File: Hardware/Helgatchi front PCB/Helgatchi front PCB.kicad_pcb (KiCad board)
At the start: 2 copper layers, 50 x 80 mm, 34 parts, among them J1 BATTERY, J2 SCREEN, M1 MOTOR, Q1 NMOS, SW1 LEFT BUTTON, SW2 CENTER BUTTON, SW3 RIGHT BUTTON, U1 XIAO ESP32-S3

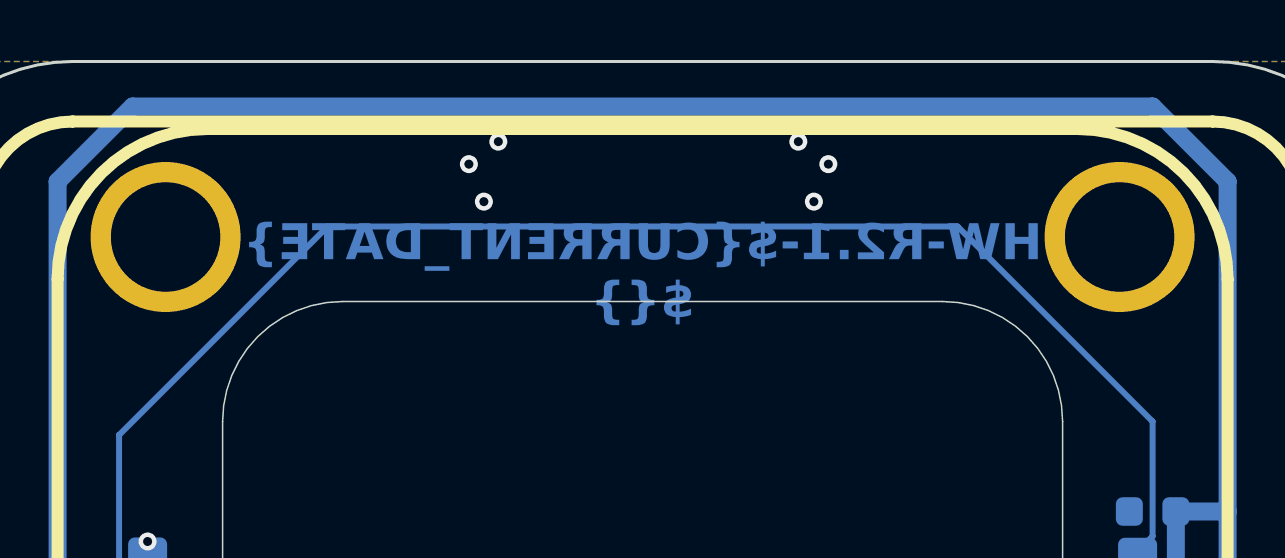
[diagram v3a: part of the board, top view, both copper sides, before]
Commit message: LCSC part # changes
- Changed MOLEX Picoblate part number out for generic picoblade
- Added part number and adjusted DNP for ESP32-S3
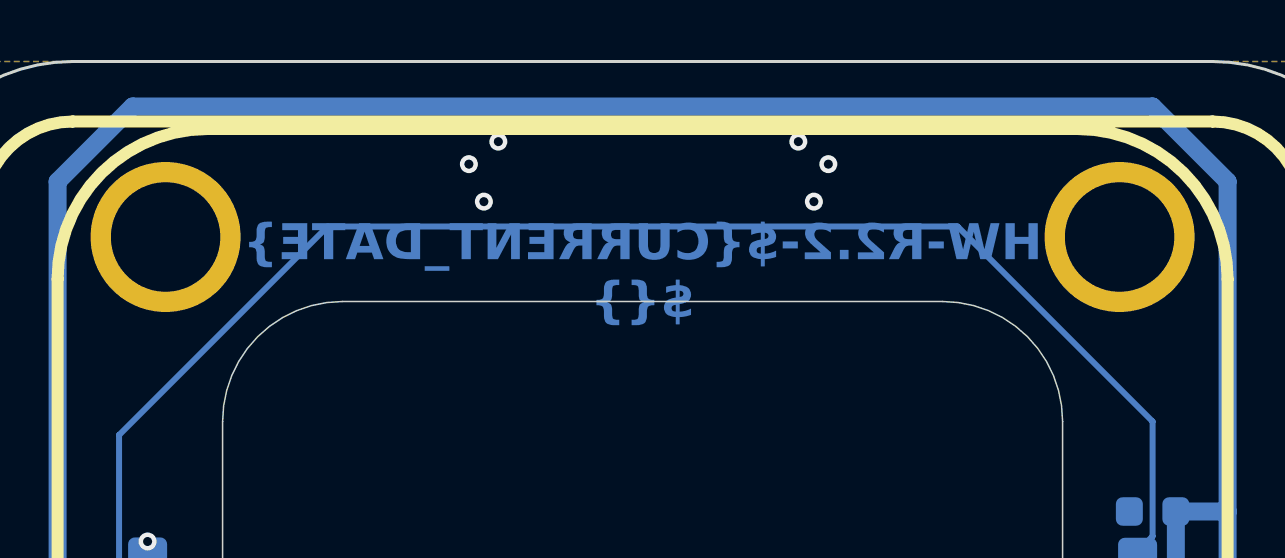
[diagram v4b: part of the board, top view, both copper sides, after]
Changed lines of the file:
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@@
 		(title "Helgatchi Front")
 		(date "2026-01-22")
-		(rev "R2.1")
+		(rev "R2.2")
 		(company "DC801 and Friends")
 	)
@@
 			)
 		)
-		(property "LCSC Part #" "C293349"
+		(property "LCSC Part #" "C7433459"
 			(at 0 0 180)
 			(unlocked yes)
@@
 			)
 		)
-		(property "LCSC Part #" ""
+		(property "LCSC Part #" "C9900124959"
 			(at 0 0 180)
 			(unlocked yes)
@@
 		(sheetname "/")
 		(sheetfile "Helgatchi front PCB.kicad_sch")
-		(attr exclude_from_bom dnp)
 		(fp_line
 			(start -8.896364 -8.56)
@@
 			(justify mirror)
 		)
-		(render_cache "HW-R2.1-2026-02-03\n" 0
+		(render_cache "HW-R2.2-2026-02-06\n" 0
 			(polygon
 				(pts
@@
 			(polygon
 				(pts
-					(xy 166.160669 65.824489) (xy 166.160669 65.243875) (xy 166.210119 65.275054) (xy 166.268087 65.303446)
-					(xy 166.370523 65.344552) (xy 166.43764 65.173387) (xy 166.350372 65.134845) (xy 166.256363 65.082822)
-					(xy 166.167337 65.022371) (xy 166.127579 64.989421) (xy 166.095163 64.956939) (xy 165.954186 64.956939)
-					(xy 165.954186 65.824489) (xy 165.74763 65.824489) (xy 165.74763 65.998) (xy 166.378876 65.998)
-					(xy 166.378876 65.824489)
+					(xy 165.789615 65.230466) (xy 165.794658 65.283159) (xy 165.809765 65.333708) (xy 165.833009 65.382098)
+					(xy 165.863474 65.430208) (xy 165.939019 65.520773) (xy 166.024675 65.604671) (xy 166.075086 65.652518)
+					(xy 166.128795 65.709598) (xy 166.171587 65.769095) (xy 166.18514 65.799208) (xy 166.189172 65.824489)
+					(xy 165.742647 65.824489) (xy 165.742647 65.998) (xy 166.420861 65.998) (xy 166.425111 65.955868)
+					(xy 166.424232 65.920477) (xy 166.416298 65.838775) (xy 166.393164 65.765505) (xy 166.357857 65.697398)
+					(xy 166.314249 65.634933) (xy 166.264595 65.577041) (xy 166.211887 65.523704) (xy 166.109451 65.425079)
+					(xy 166.064628 65.377399) (xy 166.030536 65.334147) (xy 166.006913 65.288971) (xy 165.999469 65.244828)
+					(xy 166.004145 65.203834) (xy 166.017157 65.171667) (xy 166.038084 65.146276) (xy 166.06557 65.127315)
+					(xy 166.097613 65.115739) (xy 166.135463 65.111691) (xy 166.184191 65.117297) (xy 166.237899 65.135212)
+					(xy 166.289425 65.165395) (xy 166.343631 65.214127) (xy 166.446067 65.070438) (xy 166.39862 65.02751)
+					(xy 166.347025 64.993161) (xy 166.290802 64.966904) (xy 166.20204 64.94169) (xy 166.115313 64.933491)
+					(xy 166.052505 64.938148) (xy 165.992801 64.951956) (xy 165.937061 64.975211) (xy 165.88868 65.007351)
+					(xy 165.848244 65.048694) (xy 165.816506 65.10048) (xy 165.796626 65.159704)
 				)
 			)
@@
 			(polygon
 				(pts
-					(xy 156.927117 66.021447) (xy 157.008596 66.015512) (xy 157.090809 66.001077) (xy 157.163862 65.982539)
-					(xy 157.215885 65.963928) (xy 157.175585 65.789538) (xy 157.075714 65.824782) (xy 157.011165 65.83827)
-					(xy 156.928802 65.843247) (xy 156.859632 65.83715) (xy 156.812085 65.821333) (xy 156.780278 65.798038)
-					(xy 156.756602 65.765723) (xy 156.742348 65.728766) (xy 156.737414 65.685784) (xy 156.745187 65.635112)
-					(xy 156.766794 65.598046) (xy 156.80292 65.571112) (xy 156.847738 65.553738) (xy 156.90244 65.542492)
-					(xy 156.969029 65.538432) (xy 157.03285 65.538432) (xy 157.03285 65.364922) (xy 156.95562 65.364922)
-					(xy 156.891873 65.358254) (xy 156.861245 65.34937) (xy 156.834793 65.336639) (xy 156.811937 65.319149)
-					(xy 156.793687 65.296632) (xy 156.781974 65.269347) (xy 156.777714 65.233324) (xy 156.781833 65.197039)
-					(xy 156.793404 65.167879) (xy 156.812152 65.144224) (xy 156.836903 65.12669) (xy 156.867919 65.115661)
-					(xy 156.906967 65.111691) (xy 156.965256 65.116482) (xy 157.023691 65.131035) (xy 157.078767 65.153193)
-					(xy 157.123562 65.178882) (xy 157.197421 65.026548) (xy 157.147809 64.997508) (xy 157.0774 64.964852)
-					(xy 156.999397 64.941623) (xy 156.908652 64.933491) (xy 156.824638 64.939322) (xy 156.756758 64.9554)
-					(xy 156.696622 64.982305) (xy 156.650146 65.016729) (xy 156.61361 65.059828) (xy 156.58801 65.110079)
-					(xy 156.572996 65.165403) (xy 156.56786 65.22607) (xy 156.576503 65.28646) (xy 156.603105 65.345505)
-					(xy 156.64432 65.39602) (xy 156.697114 65.432919) (xy 156.646531 65.459517) (xy 156.605222 65.492593)
-					(xy 156.572037 65.532424) (xy 156.54772 65.578081) (xy 156.532766 65.629878) (xy 156.52756 65.689228)
-					(xy 156.533597 65.759699) (xy 156.551081 65.822511) (xy 156.580818 65.87909) (xy 156.623255 65.927877)
-					(xy 156.677211 65.966713) (xy 156.747525 65.997047) (xy 156.827038 66.014909)
+					(xy 156.674564 64.956955) (xy 156.759885 64.970591) (xy 156.838091 64.992623) (xy 156.912528 65.024274)
+					(xy 156.978263 65.064029) (xy 157.03622 65.111984) (xy 157.086309 65.168012) (xy 157.128532 65.232663)
+					(xy 157.162982 65.306963) (xy 157.187055 65.385499) (xy 157.20217 65.474107) (xy 157.207459 65.574263)
+					(xy 157.200486 65.69216) (xy 157.181547 65.784915) (xy 157.152955 65.857226) (xy 157.116014 65.913003)
+					(xy 157.06667 65.959274) (xy 157.007367 65.992824) (xy 156.936066 66.013931) (xy 156.849887 66.021447)
+					(xy 156.793557 66.017543) (xy 156.744712 66.006432) (xy 156.702169 65.988694) (xy 156.645088 65.950714)
+					(xy 156.599734 65.903771) (xy 156.564651 65.849068) (xy 156.540163 65.789465) (xy 156.525569 65.727129)
+					(xy 156.521165 65.671129) (xy 156.722246 65.671129) (xy 156.729793 65.729674) (xy 156.739506 65.758608)
+					(xy 156.753314 65.784775) (xy 156.771552 65.807702) (xy 156.794493 65.826541) (xy 156.821565 65.838906)
+					(xy 156.85487 65.843247) (xy 156.895857 65.837769) (xy 156.927923 65.822364) (xy 156.953953 65.798194)
+					(xy 156.974158 65.766384) (xy 156.988221 65.729691) (xy 156.997679 65.68703) (xy 157.004347 65.594266)
+					(xy 157.003541 65.562539) (xy 157.000976 65.532424) (xy 156.945582 65.514032) (xy 156.880076 65.507364)
+					(xy 156.823491 65.512993) (xy 156.784189 65.527759) (xy 156.75749 65.550009) (xy 156.73881 65.58034)
+					(xy 156.726696 65.619851) (xy 156.722246 65.671129) (xy 156.521165 65.671129) (xy 156.520819 65.666733)
+					(xy 156.525303 65.600652) (xy 156.538478 65.538945) (xy 156.561876 65.481968) (xy 156.596363 65.433066)
+					(xy 156.641574 65.392811) (xy 156.699678 65.360745) (xy 156.766768 65.341074) (xy 156.853258 65.333854)
+					(xy 156.90704 65.341401) (xy 156.969102 65.362357) (xy 156.944871 65.301637) (xy 156.911217 65.25384)
+					(xy 156.868327 65.214558) (xy 156.818014 65.182986) (xy 156.762239 65.159577) (xy 156.700484 65.143785)
+					(xy 156.6361 65.134654) (xy 156.569472 65.130449) (xy 156.581196 64.952249)
 				)
 			)
